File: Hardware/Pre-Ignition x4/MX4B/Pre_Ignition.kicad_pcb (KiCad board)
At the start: 2 copper layers, 100 x 100 mm, 141 parts, among them IC1 L7805CDT, J2 Conn_01x04, J3 Conn_02x16_Counter_Clockwise, J4 VR_Header, J5 Conn_02x12_Counter_Clockwise, J6 Conn_02x16_Counter_Clockwise, J7 Conn_02x10_Counter_Clockwise, Q1 AO3400A, Q2 AO3400A, Q3 AO3400A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

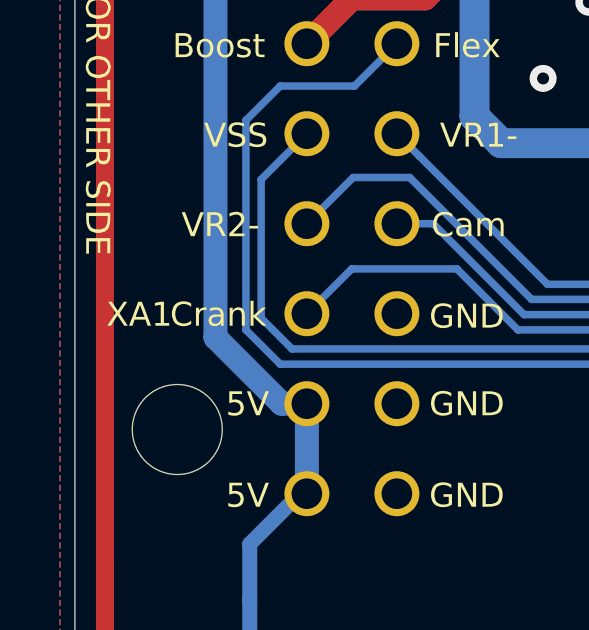
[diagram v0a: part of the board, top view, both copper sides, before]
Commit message: Pre-Ignition x2 Initial Upload, MX4B Production.
Pre-Ignition x2 Initial Upload - 2 Channel Speeduino compatible ECU
Pre-Ignition x4 MX4B (revision B) - minor updates, BOM changes, connectors moved to bottom side of board.
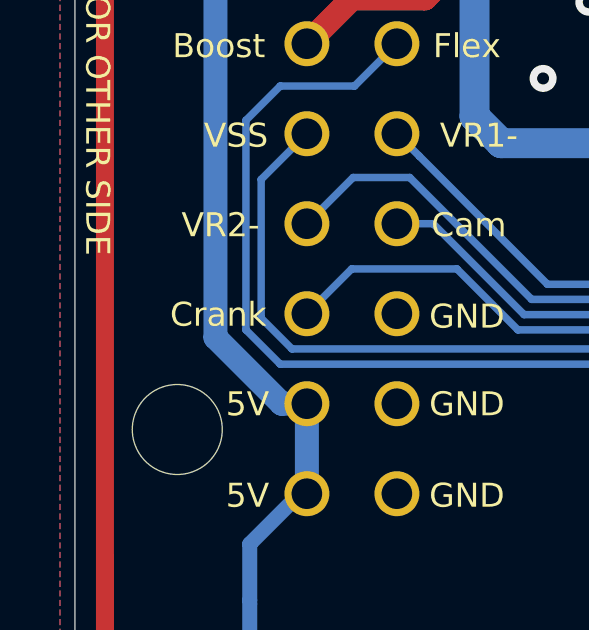
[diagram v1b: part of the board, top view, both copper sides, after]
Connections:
- A1 pad 10: Net-(A1-Pad10) -> (no net)
- A1 pad 11: Net-(A1-Pad11) -> (no net)
- A1 pad 12: Net-(A1-Pad12) -> (no net)
- A1 pad 2: Net-(A1-Pad2) -> (no net)
- J2 pad 6: Net-(J2-Pad6) -> (no net)
- J3 pad 10: Net-(J3-Pad10) -> (no net)
- J3 pad 11: Net-(J3-Pad11) -> (no net)
- J3 pad 12: Net-(J3-Pad12) -> (no net)
- J3 pad 13: Net-(J3-Pad13) -> (no net)
- J3 pad 14: Net-(J3-Pad14) -> (no net)
- J3 pad 18: Net-(J3-Pad18) -> (no net)
- J3 pad 19: Net-(J3-Pad19) -> (no net)
- J3 pad 2: Net-(J3-Pad2) -> (no net)
- J3 pad 20: Net-(J3-Pad20) -> (no net)
- J3 pad 21: Net-(J3-Pad21) -> (no net)
- J3 pad 22: Net-(J3-Pad22) -> (no net)
- J3 pad 23: Net-(J3-Pad23) -> (no net)
- J3 pad 24: Net-(J3-Pad24) -> (no net)
- J3 pad 25: Net-(J3-Pad25) -> (no net)
- J3 pad 26: Net-(J3-Pad26) -> (no net)
- J3 pad 27: Net-(J3-Pad27) -> (no net)
- J3 pad 28: Net-(J3-Pad28) -> (no net)
- J3 pad 29: Net-(J3-Pad29) -> (no net)
- J3 pad 3: Net-(J3-Pad3) -> (no net)
- J3 pad 30: Net-(J3-Pad30) -> (no net)
- J3 pad 34: Net-(J3-Pad34) -> (no net)
- J3 pad 35: Net-(J3-Pad35) -> (no net)
- J3 pad 36: Net-(J3-Pad36) -> (no net)
- J3 pad 37: Net-(J3-Pad37) -> (no net)
- J3 pad 38: Net-(J3-Pad38) -> (no net)
- J3 pad 39: Net-(J3-Pad39) -> (no net)
- J3 pad 4: Net-(J3-Pad4) -> (no net)
- J3 pad 40: Net-(J3-Pad40) -> (no net)
- J3 pad 41: Net-(J3-Pad41) -> (no net)
- J3 pad 42: Net-(J3-Pad42) -> (no net)
- J3 pad 43: Net-(J3-Pad43) -> (no net)
- J3 pad 44: Net-(J3-Pad44) -> (no net)
- J3 pad 45: Net-(J3-Pad45) -> (no net)
- J3 pad 46: Net-(J3-Pad46) -> (no net)
- J3 pad 5: Net-(J3-Pad5) -> (no net)
- J3 pad 6: Net-(J3-Pad6) -> (no net)
- J3 pad 7: Net-(J3-Pad7) -> (no net)
- J3 pad 8: Net-(J3-Pad8) -> (no net)
- J3 pad 9: Net-(J3-Pad9) -> (no net)
- J6 pad 10: Net-(J6-Pad10) -> (no net)
- J6 pad 11: Net-(J6-Pad11) -> (no net)
- J6 pad 12: Net-(J6-Pad12) -> (no net)
- J6 pad 13: Net-(J6-Pad13) -> (no net)
- J6 pad 14: Net-(J6-Pad14) -> (no net)
- J6 pad 18: Net-(J6-Pad18) -> (no net)
- J6 pad 19: Net-(J6-Pad19) -> (no net)
- J6 pad 2: Net-(J6-Pad2) -> (no net)
- J6 pad 20: Net-(J6-Pad20) -> (no net)
- J6 pad 21: Net-(J6-Pad21) -> (no net)
- J6 pad 22: Net-(J6-Pad22) -> (no net)
- J6 pad 23: Net-(J6-Pad23) -> (no net)
- J6 pad 24: Net-(J6-Pad24) -> (no net)
- J6 pad 25: Net-(J6-Pad25) -> (no net)
- J6 pad 26: Net-(J6-Pad26) -> (no net)
- J6 pad 27: Net-(J6-Pad27) -> (no net)
- J6 pad 28: Net-(J6-Pad28) -> (no net)
- J6 pad 29: Net-(J6-Pad29) -> (no net)
- J6 pad 3: Net-(J6-Pad3) -> (no net)
- J6 pad 30: Net-(J6-Pad30) -> (no net)
- J6 pad 34: Net-(J6-Pad34) -> (no net)
- J6 pad 35: Net-(J6-Pad35) -> (no net)
- J6 pad 36: Net-(J6-Pad36) -> (no net)
- J6 pad 37: Net-(J6-Pad37) -> (no net)
- J6 pad 38: Net-(J6-Pad38) -> (no net)
- J6 pad 39: Net-(J6-Pad39) -> (no net)
- J6 pad 4: Net-(J6-Pad4) -> (no net)
- J6 pad 40: Net-(J6-Pad40) -> (no net)
- J6 pad 41: Net-(J6-Pad41) -> (no net)
- J6 pad 42: Net-(J6-Pad42) -> (no net)
- J6 pad 43: Net-(J6-Pad43) -> (no net)
- J6 pad 44: Net-(J6-Pad44) -> (no net)
- J6 pad 45: Net-(J6-Pad45) -> (no net)
- J6 pad 46: Net-(J6-Pad46) -> (no net)
- J6 pad 5: Net-(J6-Pad5) -> (no net)
- J6 pad 6: Net-(J6-Pad6) -> (no net)
- J6 pad 7: Net-(J6-Pad7) -> (no net)
- J6 pad 8: Net-(J6-Pad8) -> (no net)
- J6 pad 9: Net-(J6-Pad9) -> (no net)
- Map1 pad 1: Net-(Map1-Pad1) -> (no net)
- Map1 pad 5: Net-(Map1-Pad5) -> (no net)
- Map1 pad 6: Net-(Map1-Pad6) -> (no net)
- Map1 pad 7: Net-(Map1-Pad7) -> (no net)
- Map1 pad 8: Net-(Map1-Pad8) -> (no net)
- U1 pad 1: Net-(U1-Pad1) -> (no net)
- U1 pad 8: Net-(U1-Pad8) -> (no net)
- U2 pad 1: Net-(U2-Pad1) -> (no net)
- U2 pad 8: Net-(U2-Pad8) -> (no net)
- U5 pad 1: TVS10 -> (no net)
- U5 pad 4: TVS11 -> (no net)
- U5 pad 6: TVS12 -> (no net)
- U6 pad 4: TVS15 -> (no net)
- U6 pad 6: TVS16 -> (no net)
- U7 pad 14: Net-(U7-Pad14) -> (no net)
- U7 pad 3: Net-(U7-Pad3) -> (no net)
- XA1 pad 3V3: +3V3 -> (no net)
- XA1 pad A11: MC-A11 -> (no net)
- XA1 pad A12: MC-A12 -> (no net)
- XA1 pad A13: MC-A13 -> (no net)
- XA1 pad A6: MC-A6 -> (no net)
- XA1 pad A7: MC-A7 -> (no net)
- XA1 pad AREF: MC-AREF -> (no net)
- XA1 pad D12: MC-D12 -> (no net)
- XA1 pad D13: MC-D13 -> (no net)
- XA1 pad D14: MC-D14 -> (no net)
- XA1 pad D15: MC-D15 -> (no net)
- XA1 pad D22: MC-D22 -> (no net)
- XA1 pad D23: MC-D23 -> (no net)
- XA1 pad D25: MC-D25 -> (no net)
- XA1 pad D26: MC-D26 -> (no net)
- XA1 pad D27: MC-D27 -> (no net)
- XA1 pad D28: MC-D28 -> (no net)
- XA1 pad D29: MC-D29 -> (no net)
- XA1 pad D30: MC-D30 -> (no net)
- XA1 pad D31: MC-D31 -> (no net)
- XA1 pad D32: MC-D32 -> (no net)
- XA1 pad D33: MC-D33 -> (no net)
- XA1 pad D34: MC-D34 -> (no net)
- XA1 pad D35: MC-D35 -> (no net)
- XA1 pad D36: MC-D36 -> (no net)
- XA1 pad D37: MC-D37 -> (no net)
- XA1 pad D43: MC-D43 -> (no net)
- XA1 pad D48: MC-D48 -> (no net)
- XA1 pad IORF: MC-IOREF -> (no net)
- XA1 pad SCL: MC-SCL -> (no net)
- XA1 pad SDA: MC-SDA -> (no net)
- XA1 pad VIN: Net-(XA1-PadVIN) -> (no net)

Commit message: bom fix
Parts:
- R34, R61: value 470 -> 220
